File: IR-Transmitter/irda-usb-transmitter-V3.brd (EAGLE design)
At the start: 50 x 50 mm, 22 parts, among them IC1 FT232RL, IC2 MCP2120, Q2 7.3728MHz

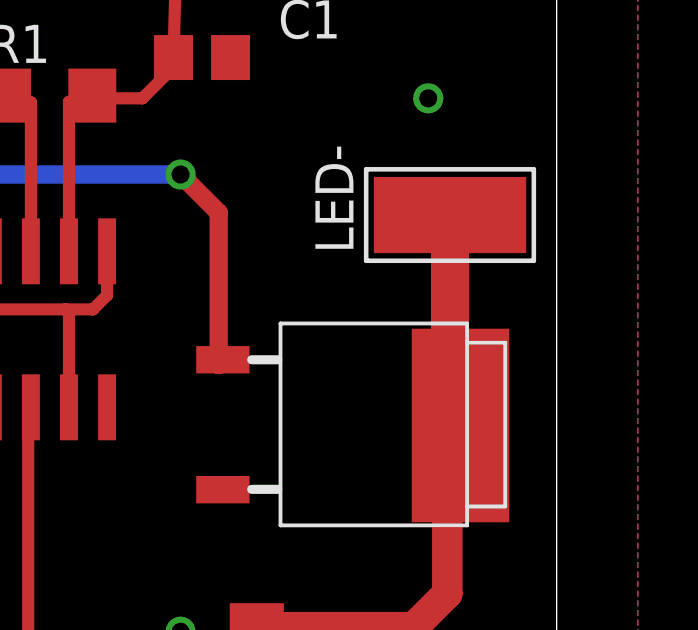
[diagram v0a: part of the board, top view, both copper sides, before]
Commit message: Updated Board layouts an schematics
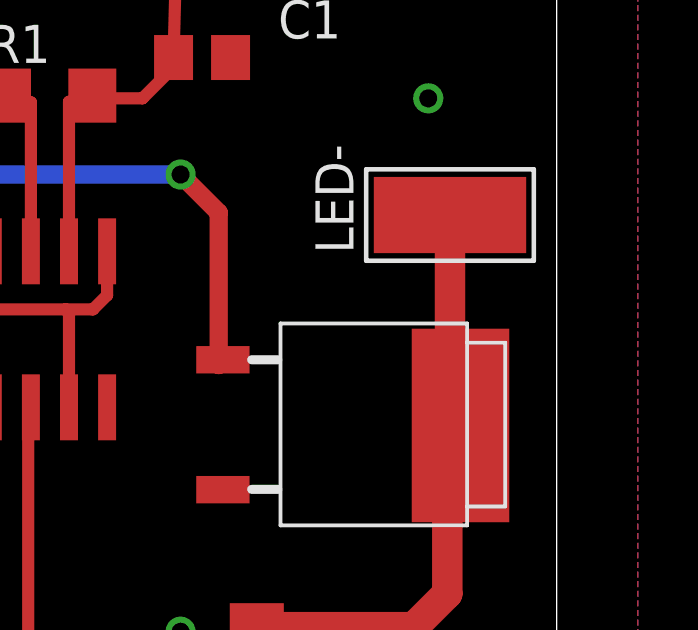
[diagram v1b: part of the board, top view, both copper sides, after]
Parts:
- renumbered U$1 to T1
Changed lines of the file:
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@@
 <element name="H3" library="holes" package="2,8" value="MOUNT-HOLE2.8" x="12.65" y="4"/>
 <element name="H4" library="holes" package="2,8" value="MOUNT-HOLE2.8" x="45.76" y="4"/>
-<element name="U$1" library="international" package="D-PAK" value="IRLR3915PBF" x="43.905" y="27.86" smashed="yes" rot="R270"/>
+<element name="T1" library="international" package="D-PAK" value="IRLR3915PBF" x="43.905" y="27.86" smashed="yes" rot="R270"/>
 <element name="IC2" library="microchip" package="SO-14" value="MCP2120" x="31.205" y="31.035" smashed="yes" rot="R180">
 <attribute name="NAME" x="26.453" y="30.56" size="1.27" layer="25" rot="R90"/>
@@
 <contactref element="IC1" pad="26"/>
 <contactref element="USB" pad="GND"/>
-<contactref element="U$1" pad="S"/>
+<contactref element="T1" pad="S"/>
 <contactref element="GND" pad="1"/>
 <contactref element="IC2" pad="5"/>
@@
 </signal>
 <signal name="IRLEDS-">
-<contactref element="LED-" pad="1"/>
-<contactref element="U$1" pad="D"/>
-<wire x1="46.445" y1="34.845" x2="46.445" y2="28.18" width="1.27" layer="1"/>
+<contactref element="T1" pad="D"/>
 <wire x1="46.445" y1="28.18" x2="46.795" y2="27.83" width="1.27" layer="1"/>
 <contactref element="R3" pad="1"/>
@@
 <wire x1="46.355" y1="22.225" x2="46.355" y2="27.39" width="1.016" layer="1"/>
 <wire x1="46.355" y1="27.39" x2="46.795" y2="27.83" width="1.016" layer="1"/>
+<contactref element="LED-" pad="1"/>
+<wire x1="46.445" y1="34.845" x2="46.445" y2="28.18" width="1.016" layer="1"/>
 </signal>
 <signal name="+3V3">
@@
 <signal name="TXIR">
 <contactref element="IC2" pad="6"/>
-<contactref element="U$1" pad="G"/>
+<contactref element="T1" pad="G"/>
 <wire x1="28.665" y1="33.635" x2="28.665" y2="35.65" width="0.6096" layer="1"/>
 <wire x1="28.665" y1="35.65" x2="28.575" y2="36.195" width="0.6096" layer="1"/>
@@
 </signal>
 <signal name="N$1">
-<contactref element="LED+" pad="1"/>
 <contactref element="R2" pad="1"/>
 <contactref element="R3" pad="2"/>
@@
 <wire x1="39.37" y1="15.24" x2="40.005" y2="15.875" width="1.016" layer="1"/>
 <wire x1="40.005" y1="15.875" x2="40.005" y2="18.263" width="1.016" layer="1"/>
+<wire x1="40.568" y1="17.7" x2="40.005" y2="18.263" width="1.016" layer="1"/>
+<contactref element="LED+" pad="1"/>
 <wire x1="46.445" y1="17.7" x2="40.568" y2="17.7" width="1.016" layer="1"/>
-<wire x1="40.568" y1="17.7" x2="40.005" y2="18.263" width="1.016" layer="1"/>
 </signal>
 </signals>

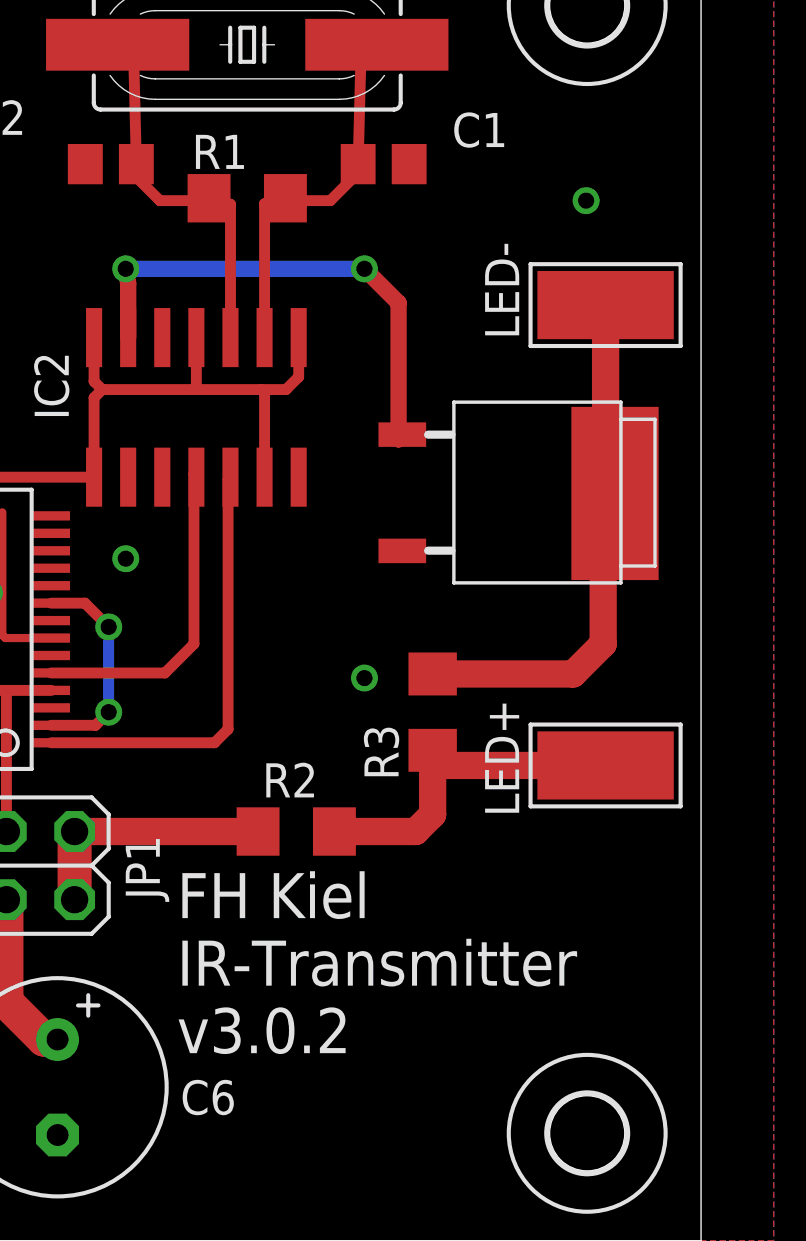
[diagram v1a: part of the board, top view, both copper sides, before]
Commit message: Fixed layout errors. Layout is now tested.
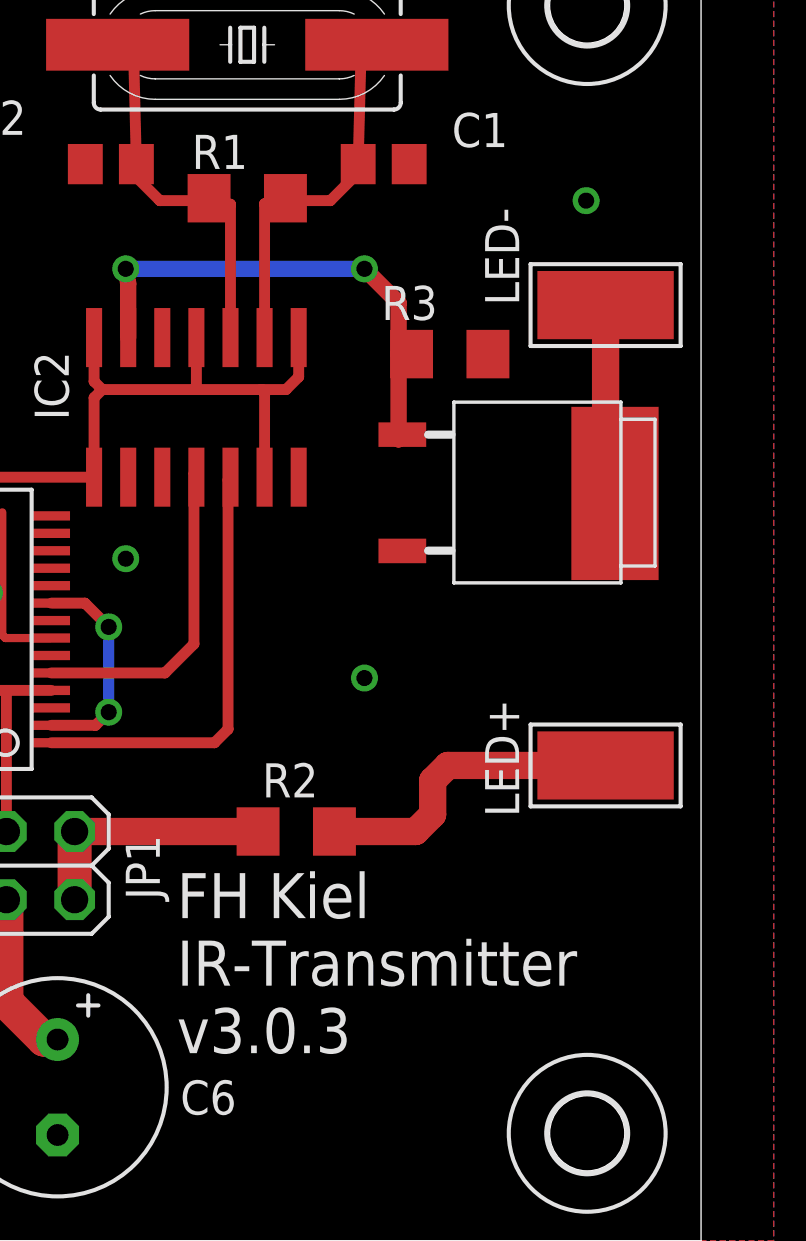
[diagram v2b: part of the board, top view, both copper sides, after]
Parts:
- R3: value (none) -> 1k
- moved R3 13.4 mm to (40.6, 33.0), turned to 180 degrees
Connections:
- net GND: now also R3.1
- net IRLEDS-: no longer R3.1
- net N$1: no longer R3.2
- net TXIR: now also R3.2
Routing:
- net IRLEDS-: track 19.8 -> 7.16 mm
- net N$1: track 13.0 -> 11.9 mm
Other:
- board text added: "FH Kiel IR-Transmitter v3.0.3"
- board text removed: "FH Kiel IR-Transmitter v3.0.2"
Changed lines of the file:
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@@
 <text x="30.48" y="6.985" size="1.6764" layer="25" font="vector">FH Kiel
 IR-Transmitter
-v3.0.2</text>
+v3.0.3</text>
 <text x="22.225" y="15.875" size="1.27" layer="25" rot="R180">V_USB</text>
 <text x="22.225" y="13.335" size="1.27" layer="25" rot="R180">V+</text>
@@
 </element>
 <element name="LED-" library="wirepad" package="5-2,5" value="IR-LED" x="46.445" y="34.845" smashed="yes" rot="R90">
-<attribute name="NAME" x="43.227" y="33.565" size="1.27" layer="25" ratio="10" rot="R90"/>
+<attribute name="NAME" x="43.227" y="34.835" size="1.27" layer="25" ratio="10" rot="R90"/>
 <attribute name="VALUE" x="43.645" y="34.745" size="0.0254" layer="27" rot="R90"/>
 </element>
@@
 <attribute name="VALUE" x="36.195" y="17.78" size="1.27" layer="27" rot="R180"/>
 </element>
-<element name="R3" library="rcl" package="R1206" value="" x="40.005" y="19.685" smashed="yes" rot="R270">
-<attribute name="NAME" x="38.735" y="17.145" size="1.27" layer="25" rot="R90"/>
-<attribute name="VALUE" x="37.465" y="20.955" size="1.27" layer="27" rot="R270"/>
+<element name="R3" library="rcl" package="R1206" value="1k" x="40.64" y="33.02" smashed="yes" rot="R180">
+<attribute name="NAME" x="38.1" y="34.29" size="1.27" layer="25"/>
+<attribute name="VALUE" x="38.1" y="31.75" size="1.27" layer="27" rot="R90"/>
 </element>
 </elements>
@@
 <via x="37.465" y="20.955" extent="1-16" drill="0.6" shape="square"/>
 <via x="45.72" y="38.735" extent="1-16" drill="0.6" shape="square"/>
+<contactref element="R3" pad="1"/>
 </signal>
 <signal name="D+">
@@
 <contactref element="T1" pad="D"/>
 <wire x1="46.445" y1="28.18" x2="46.795" y2="27.83" width="1.27" layer="1"/>
-<contactref element="R3" pad="1"/>
-<wire x1="40.005" y1="21.107" x2="45.237" y2="21.107" width="1.016" layer="1"/>
-<wire x1="45.237" y1="21.107" x2="46.355" y2="22.225" width="1.016" layer="1"/>
-<wire x1="46.355" y1="22.225" x2="46.355" y2="27.39" width="1.016" layer="1"/>
-<wire x1="46.355" y1="27.39" x2="46.795" y2="27.83" width="1.016" layer="1"/>
 <contactref element="LED-" pad="1"/>
 <wire x1="46.445" y1="34.845" x2="46.445" y2="28.18" width="1.016" layer="1"/>
@@
 <via x="37.465" y="36.195" extent="1-16" drill="0.6" shape="square"/>
 <wire x1="37.465" y1="36.195" x2="38.735" y2="34.925" width="0.6096" layer="1"/>
-<wire x1="38.735" y1="34.925" x2="38.735" y2="29.845" width="0.6096" layer="1"/>
+<wire x1="38.735" y1="34.925" x2="38.735" y2="33.02" width="0.6096" layer="1"/>
+<wire x1="38.735" y1="33.02" x2="38.735" y2="29.845" width="0.6096" layer="1"/>
 <wire x1="38.875" y1="30.02" x2="38.875" y2="29.985" width="0.6096" layer="1"/>
 <wire x1="38.875" y1="29.985" x2="38.735" y2="29.845" width="0.6096" layer="1"/>
+<contactref element="R3" pad="2"/>
+<wire x1="39.218" y1="33.02" x2="38.735" y2="33.02" width="0.6096" layer="1"/>
 </signal>
 <signal name="VCCIO">
@@
 <signal name="N$1">
 <contactref element="R2" pad="1"/>
-<contactref element="R3" pad="2"/>
 <wire x1="36.347" y1="15.24" x2="39.37" y2="15.24" width="1.016" layer="1"/>
 <wire x1="39.37" y1="15.24" x2="40.005" y2="15.875" width="1.016" layer="1"/>
-<wire x1="40.005" y1="15.875" x2="40.005" y2="18.263" width="1.016" layer="1"/>
-<wire x1="40.568" y1="17.7" x2="40.005" y2="18.263" width="1.016" layer="1"/>
 <contactref element="LED+" pad="1"/>
 <wire x1="46.445" y1="17.7" x2="40.568" y2="17.7" width="1.016" layer="1"/>
+<wire x1="40.005" y1="15.875" x2="40.005" y2="17.137" width="1.016" layer="1"/>
+<wire x1="40.005" y1="17.137" x2="40.568" y2="17.7" width="1.016" layer="1"/>
 </signal>
 </signals>
